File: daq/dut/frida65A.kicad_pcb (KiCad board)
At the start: 4 copper layers, 100 x 100 mm, 92 parts, among them J1 SMA Molex 733910070, J10 CFG VIN_EXT, J11 SPI TP, J12 TP CLOCKS, J15 TP AMP, J2 SMA Molex 733910070, J3 SMA Molex 733910070, J4 RJ45 Molex 446200002, J5 DisplayPort Molex 472720024, J6 MiniFitJr Molex 469990014, J7 POWER, J8 CFG VIN_P, J9 CFG VIN_P, Q1 Q_PMOS_DGS, U1 ASIC FRIDA 65A, U2 LevelShifter TI TXV0106Q1, U3 DiffAmp TI THS4541

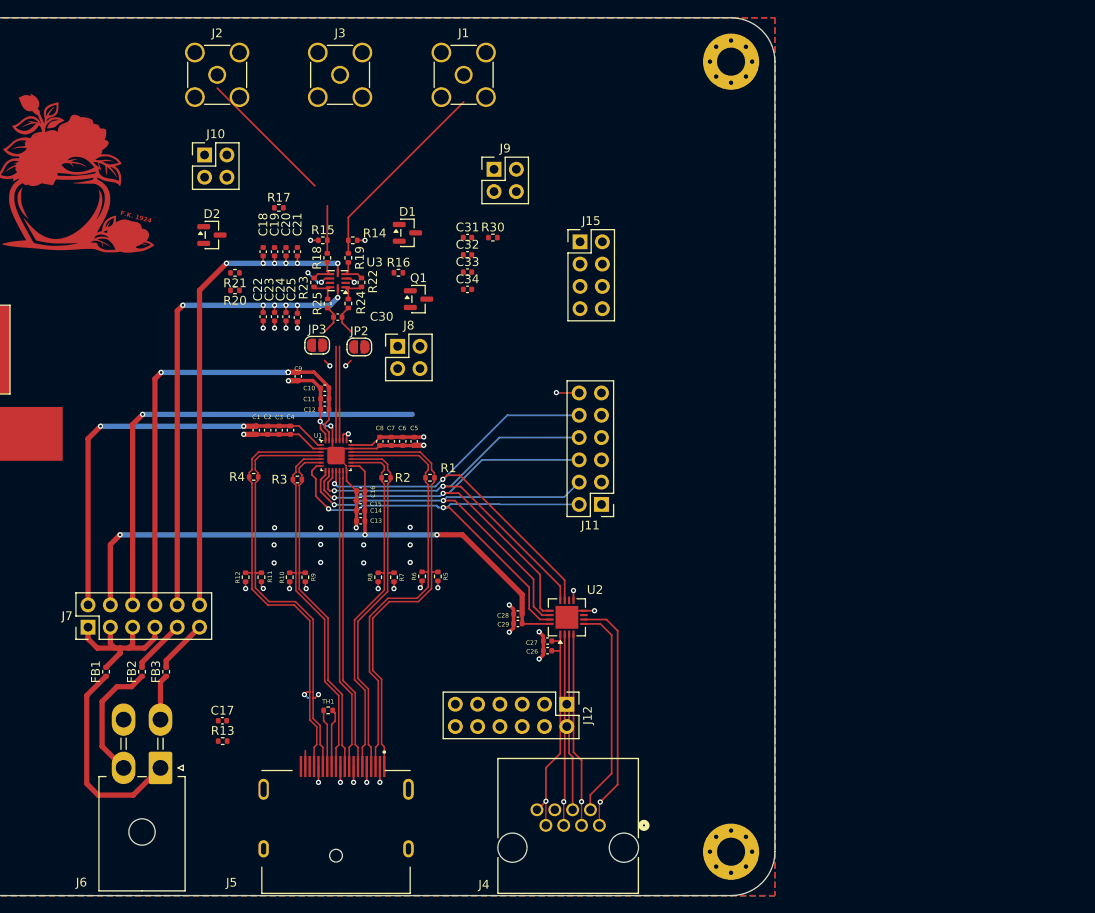
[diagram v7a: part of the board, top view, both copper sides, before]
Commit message: Add new layout generator files and update board and docs files
Add new flow/layout files for parameter classes, tech layer mapping, raw export, MOSFET generator, and MOMCAP generator, and remove old layout files that are no longer used. Update IHP130 layout metadata and inline test setup, update pytest discovery for inline layout tests, update the three PDK submodule pointers to their new commits, update DAQ KiCad project files, and remove old docs files and env.sh.
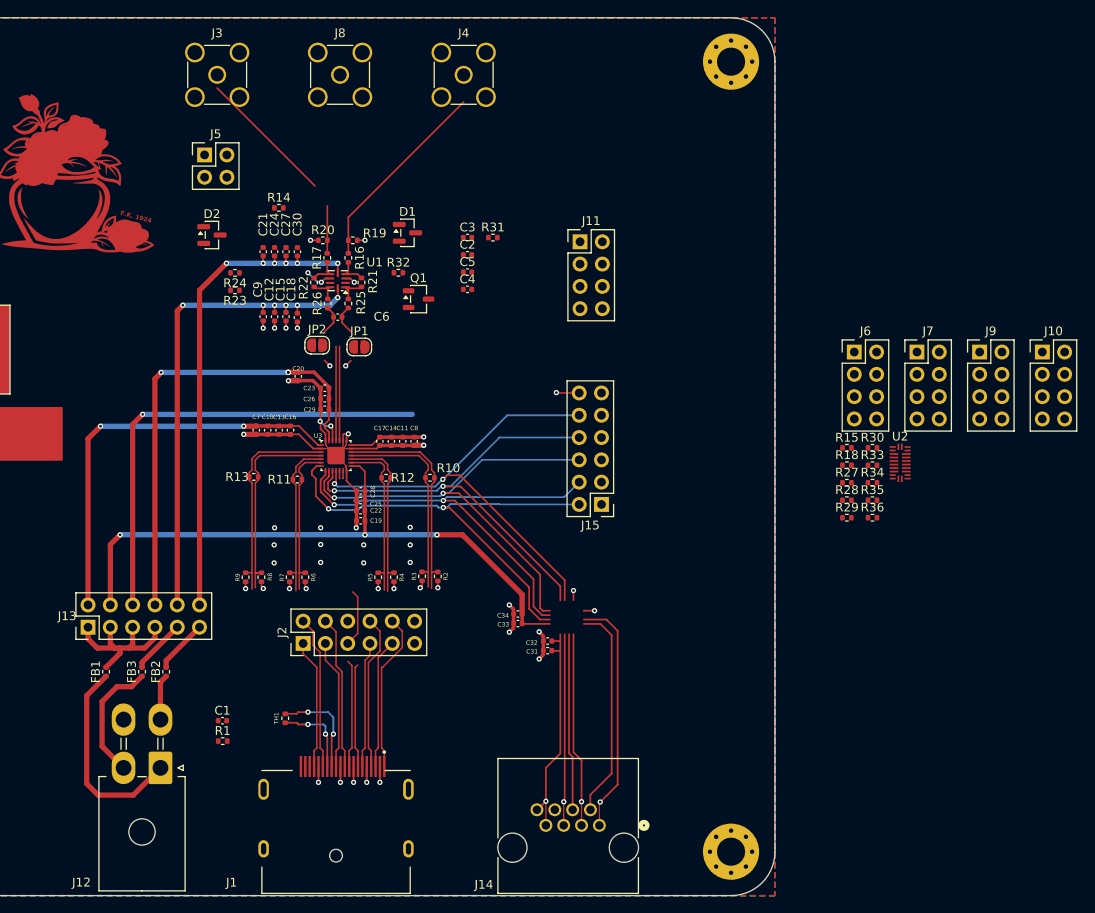
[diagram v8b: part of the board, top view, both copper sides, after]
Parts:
- removed the J8 at (157.0, 87.4)
- added J10: VIN CFG, Connector_PinHeader_2.54mm:PinHeader_2x04_P2.54mm_Vertical, F.Cu at (230.5, 88.1)
- added J6: TERM CFG, Connector_PinHeader_2.54mm:PinHeader_2x04_P2.54mm_Vertical, F.Cu at (209.0, 88.1)
- added J7: ATTEN CFG, Connector_PinHeader_2.54mm:PinHeader_2x04_P2.54mm_Vertical, F.Cu at (216.2, 88.1)
- added R15: DNP, Resistor_SMD:R_0402_1005Metric, F.Cu at (208.2, 99.0)
- added R18: DNP, Resistor_SMD:R_0402_1005Metric, F.Cu at (208.2, 101.0)
- added R27: DNP, Resistor_SMD:R_0402_1005Metric, F.Cu at (208.2, 103.0)
- added R28: DNP, Resistor_SMD:R_0402_1005Metric, F.Cu at (208.2, 105.0)
- added R29: DNP, Resistor_SMD:R_0402_1005Metric, F.Cu at (208.2, 107.0)
- added R30: DNP, Resistor_SMD:R_0402_1005Metric, F.Cu at (211.1, 99.0)
- added R33: 10k, Resistor_SMD:R_0402_1005Metric, F.Cu at (211.1, 101.0)
- added R34: 10k, Resistor_SMD:R_0402_1005Metric, F.Cu at (211.1, 103.0)
- added R35: 10k, Resistor_SMD:R_0402_1005Metric, F.Cu at (211.1, 105.0)
- added R36: 10k, Resistor_SMD:R_0402_1005Metric, F.Cu at (211.1, 107.0)
- J5: renamed from J10; value CFG VIN_EXT -> DIFF/SE CFG
- J9: value CFG VIN_P -> TERM CFG; footprint Connector_PinHeader_2.54mm:PinHeader_2x02_P2.54mm_Vertical -> Connector_PinHeader_2.54mm:PinHeader_2x04_P2.54mm_Vertical
- Q1: footprint Package_TO_SOT_SMD:SOT-23 -> Package_TO_SOT_SMD:SOT-23-3
- U2: value LevelShifter TI TXV0106Q1 -> TI LevelShifter SN74AXC8T245RJWR; footprint frida:TI_LevelShifter_TXV0106Q1 -> frida:TI_LevelShifter_SN74AXC8T245RJWR
- moved J9 59.1 mm to (223.3, 88.1)
- moved U2 41.8 mm to (214.3, 100.7), turned to 0 degrees
- moved J2 30.8 mm to (146.2, 121.3), turned to 90 degrees
- moved TH1 4.97 mm to (144.2, 129.8), turned to -90 degrees
- renumbered C17 to C1, C2 to C10, C6 to C11, C23 to C12, C3 to C13, C7 to C14, C24 to C15, C4 to C16, C8 to C17, C25 to C18, C13 to C19, C32 to C2, C9 to C20, C18 to C21, C14 to C22, C10 to C23, C19 to C24, C15 to C25, C11 to C26, C20 to C27, C16 to C28, C12 to C29, C31 to C3, C21 to C30, C26 to C31, C27 to C32, C29 to C33, C28 to C34, C34 to C4, C33 to C5, C30 to C6, C1 to C7, C5 to C8, C22 to C9, FB3 to FB2, FB2 to FB3, H3 to H2, H2 to H3, J5 to J1, J15 to J11, J6 to J12, J7 to J13, J4 to J14, J11 to J15, J12 to J2, J2 to J3, J1 to J4, J3 to J8, JP2 to JP1, JP3 to JP2, R13 to R1, R1 to R10, R3 to R11, R2 to R12, R4 to R13, R17 to R14, R19 to R16, R18 to R17, R14 to R19, R5 to R2, R15 to R20, R22 to R21, R23 to R22, R20 to R23, R21 to R24, R24 to R25, R25 to R26, R6 to R3, R30 to R31, R16 to R32, R7 to R4, R8 to R5, R9 to R6, R10 to R7, R11 to R8, R12 to R9, U3 to U1, U1 to U3
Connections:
- C4 pad 1: Net-(U3-IN+) -> Net-(J7-Pin_2)
- C5 pad 1: Net-(U3-IN-) -> Net-(J7-Pin_6)
- C6 pad 2: Net-(J9-Pin_1) -> Net-(J10-Pin_5)
- J2 pad 10: /CLK_COMP_N -> /CLK_COMP_P
- J2 pad 5: /COMP_OUT_P -> /COMP_OUT_N
- J2 pad 6: /COMP_OUT_N -> /COMP_OUT_P
- J2 pad 7: /CLK_LOGIC_P -> /CLK_LOGIC_N
- J2 pad 8: /CLK_LOGIC_N -> /CLK_LOGIC_P
- J2 pad 9: /CLK_COMP_P -> /CLK_COMP_N
- J5 pad 2: Net-(J10-Pin_2) -> Net-(J5-Pin_2)
- J5 pad 4: Net-(J10-Pin_2) -> Net-(J5-Pin_2)
- J9 pad 1: Net-(J9-Pin_1) -> GND
- J9 pad 2: /VIN_P -> Net-(J9-Pin_2)
- J9 pad 3: /VIN_P_EXT -> /VOCM_EXT
- J9 pad 4: /VIN_P -> Net-(J9-Pin_2)
- R16 pad 1: Net-(U3-IN+) -> Net-(J7-Pin_3)
- R17 pad 1: Net-(U3-IN-) -> Net-(J7-Pin_5)
- R17 pad 2: Net-(J10-Pin_2) -> Net-(J5-Pin_2)
- R19 pad 2: /VIN_P_EXT -> Net-(J6-Pin_6)
- R20 pad 2: Net-(J10-Pin_2) -> Net-(J6-Pin_2)
- R21 pad 2: Net-(U3-IN+) -> Net-(J7-Pin_2)
- R22 pad 2: Net-(U3-IN-) -> Net-(J7-Pin_6)
- R23 pad 1: /VOCM_EXT -> Net-(J9-Pin_2)
- R24 pad 2: /VOCM_EXT -> Net-(J9-Pin_6)
- R26 pad 1: Net-(J9-Pin_1) -> Net-(J10-Pin_5)
- U1 pad 4: Net-(U3-IN+) -> Net-(J7-Pin_2)
- U1 pad 6: Net-(U3-IN-) -> Net-(J7-Pin_6)
- U2 pad 1: /VDD_BDAQ -> Net-(U2-DIR1)
- U2 pad 10: unconnected-(U2-B6-Pad10) -> Net-(U2-DIR2)
- U2 pad 11: /SPI_CS_B -> GND
- U2 pad 12: /SPI_SDO -> GND
- U2 pad 13: /SPI_SDI -> GND
- U2 pad 14: /SPI_SCLK -> GND
- U2 pad 15: /RST_B -> GND
- U2 pad 16: /VDD_IO -> /SPI_SDO
- U2 pad 17: GND -> /SPI_CS_B
- U2 pad 5: /SPI_SDO_EXT -> /SPI_CS_B_EXT
- U2 pad 6: /SPI_CS_B_EXT -> /SPI_SDO_EXT
- U2 pad 8: GND -> unconnected-(U2-A7-Pad8)
- U2 pad 9: GND -> unconnected-(U2-A8-Pad9)
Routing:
- net /COMP_OUT_P: track 34.8 -> 13.2 mm
- net /COMP_OUT_N: track 34.8 -> 19.3 mm
- net (no net): track 0.00 -> 12.3 mm
- net /CLK_INIT_P: track 51.0 -> 38.8 mm, vias 1 -> 0
- net /CLK_COMP_N: track 50.2 -> 38.9 mm
- net /CLK_INIT_N: track 49.6 -> 40.7 mm, vias 1 -> 0
- net /CLK_LOGIC_N: track 41.6 -> 33.5 mm
- net /CLK_SAMP_P: track 40.8 -> 33.1 mm
- net /CLK_COMP_P: track 50.8 -> 43.1 mm
- net Net-(J10-Pin_2): track 5.42 -> 0.00 mm
- net /CLK_SAMP_N: track 40.2 -> 35.0 mm
- net Net-(J1-Pad13): track 6.68 -> 11.5 mm, vias 0 -> 2
- net /CLK_LOGIC_P: track 42.2 -> 37.6 mm
- net Net-(U3-IN-): track 3.46 -> 0.00 mm
- net Net-(U3-IN+): track 3.46 -> 0.00 mm
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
